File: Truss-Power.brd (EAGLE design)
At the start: 40.3 x 20.3 mm, 28 parts, among them J1 XF2L-0535-1, U1 TPS61090, U2 MCP73831T-2ACI/OT, U3 LC709203, U4 LC709203, U5 SC4501, X2 MicroB, X3 22-23-2021

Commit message: Schematics/Board file commit
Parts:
- removed C5: TANT-CAP, NewPart:7343-METRIC
- removed L2: CDRH5D28, NewPart:CDRH5D28
- removed U3: LC709203, NewPart:WDFN8
- removed U5: SC4501, NewPart:MSOP8
- moved J1 3.95 mm to (6.10, 3.56), turned to 90 degrees
- moved R10 1.44 mm to (9.73, 8.27), turned to 0 degrees
- moved R8 1.40 mm to (13.7, 6.88), turned to 0 degrees
- moved CN1 0.25 mm to (3.56, 15.7), flipped to the bottom, turned to 270 degrees
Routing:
- net SCL: track 12.1 -> 10.5 mm, vias 2 -> 0
- net VCC: track 11.8 -> 11.6 mm, vias 0 -> 2

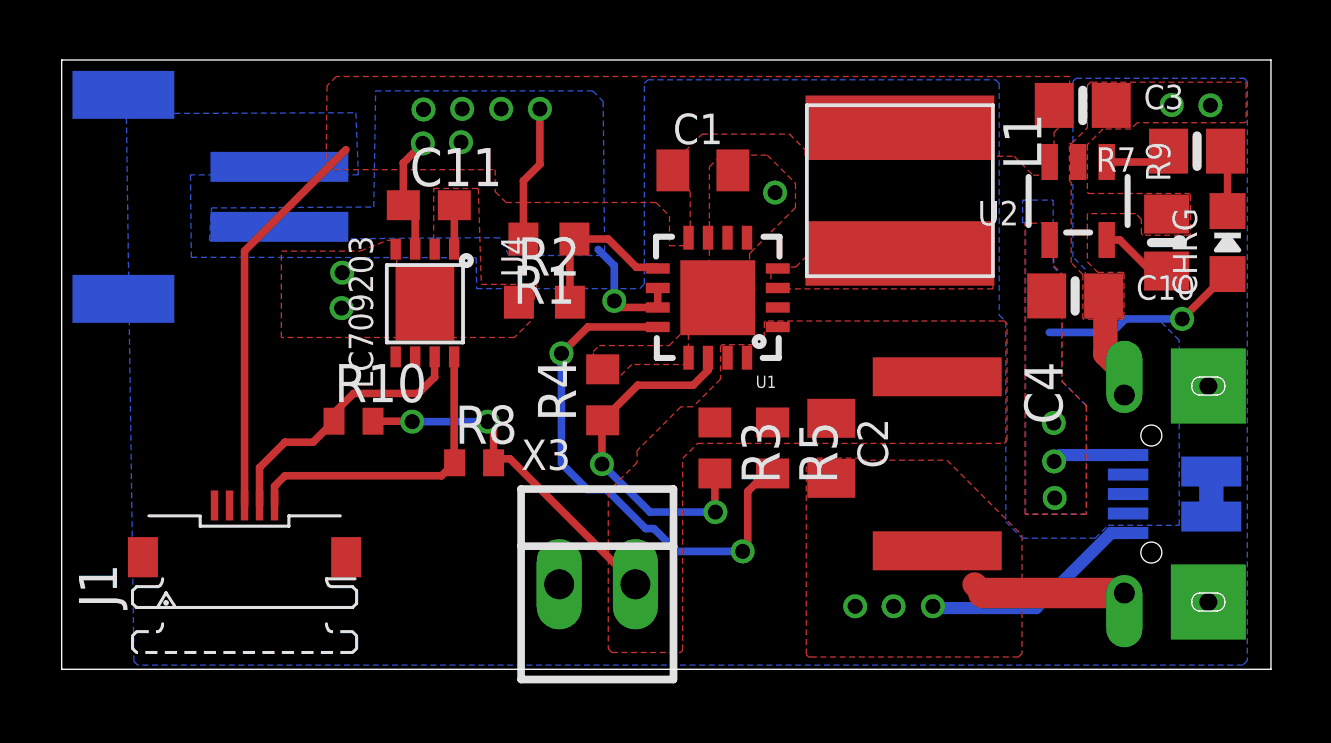
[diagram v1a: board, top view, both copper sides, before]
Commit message: Battery Connector Position Change
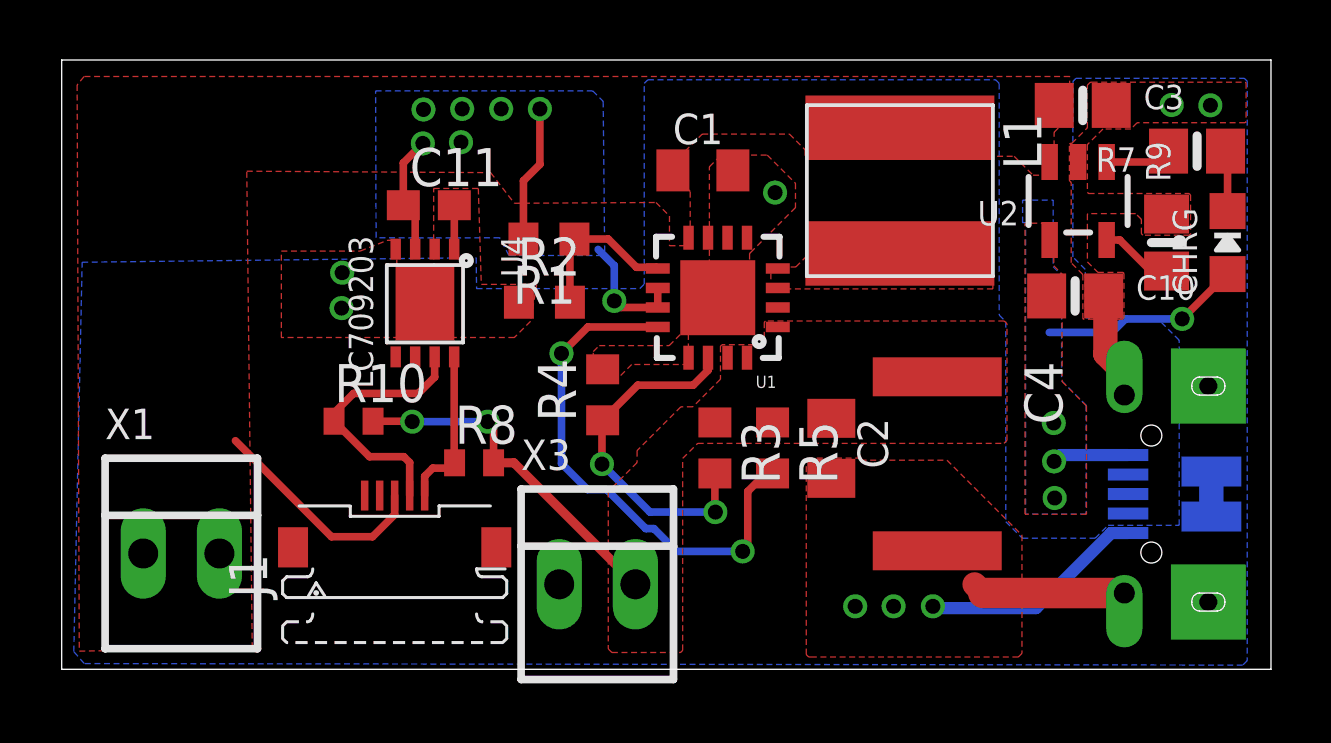
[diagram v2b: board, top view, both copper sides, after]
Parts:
- removed CN1: (no value), adafruit:JST-PH-2-SMT-RA
- added X1: 22-23-2021, con-molex:22-23-2021
- moved J1 5.01 mm to (11.1, 3.89)
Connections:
- net GND: now also X1.2; no longer CN1.2
- net VBAT: now also X1.1; no longer CN1.1
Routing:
- net VBAT: track 25.9 -> 20.2 mm
- net SCL: track 10.5 -> 5.36 mm

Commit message: TrussPower V2
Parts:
- removed U4: LC709203, NewPart:WDFN8
- added C5: 1uF, rcl:C0603
- added LED1: (no value), led:CHIP-LED0603
- added R11: 180, resistor:R0402
- added R12: 4.7K, resistor:R0402
- added R13: 330, resistor:R0402
- added R6: 1K, resistor:R0402
- added U3: MAX17044, NewPart:TDFN
- C11: value 1uF -> 10nF
- R10, R8: value 10K -> 4.7K
- R7: device microbuilder:0805-NO -> resistor:R0402
- moved J1 9.83 mm to (4.49, 11.2), flipped to the bottom
- moved R10 2.49 mm to (9.58, 5.78)
- moved R8 2.00 mm to (11.8, 7.16)
- moved C11 1.57 mm to (10.7, 15.7)
- moved R7 1.22 mm to (36.7, 17.0), turned to 0 degrees
- moved X1 0.85 mm to (3.14, 3.77)
- moved X2 0.36 mm to (36.0, 5.89)
- flipped CHRG to the bottom
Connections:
- new net ALRT: J1.2, R12.2, U3.5
- new net LEDSOC: J1.1, LED1.A
- new net N$1: C5.1, R6.2, U3.2
- new net N$3: C11.1, R11.2, U3.3
- new net N$4: LED1.C, R13.2
- net GND: now also C5.2, R13.1, U3.1, U3.4, U3.6, U3.9; no longer U4.1, U4.2, U4.4, U4.9
- net N$12: now also R7.2; no longer R7.1
- net N$13: now also R7.1; no longer R7.2
- net SCL: now also R10.1, U3.7; no longer R8.1, U4.8
- net SDA: now also R8.1, U3.8; no longer R10.1, U4.7
- net VBAT: now also R11.1, R6.1; no longer C11.1, U4.3
- net VCC: now also R12.1
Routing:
- net SCL: track 5.36 -> 16.3 mm, vias 0 -> 1
- net ALRT: track 0.00 -> 8.52 mm, vias 0 -> 1
- net VCC: track 11.7 -> 18.5 mm
- net LEDSOC: track 0.00 -> 6.32 mm
- net SDA: track 8.99 -> 14.8 mm, vias 0 -> 1
- net N$1: track 0.00 -> 5.55 mm
- net N$4: track 0.00 -> 4.78 mm
- net N$3: track 0.00 -> 4.55 mm
- net VBAT: track 20.2 -> 16.0 mm, vias 7 -> 8
- net N$12: track 2.03 -> 3.20 mm, vias 0 -> 1
- net N$13: track 2.21 -> 1.20 mm
- net GND: track 19.2 -> 19.8 mm
- net VBUS: track 9.30 -> 9.52 mm, vias 4 -> 3
